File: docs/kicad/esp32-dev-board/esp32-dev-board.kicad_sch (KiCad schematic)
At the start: 6 parts, among them K1 2-Ch Relay Module, U1 ESP32 Dev Board, U2 DS18B20 Solar, U3 DS18B20 Pool

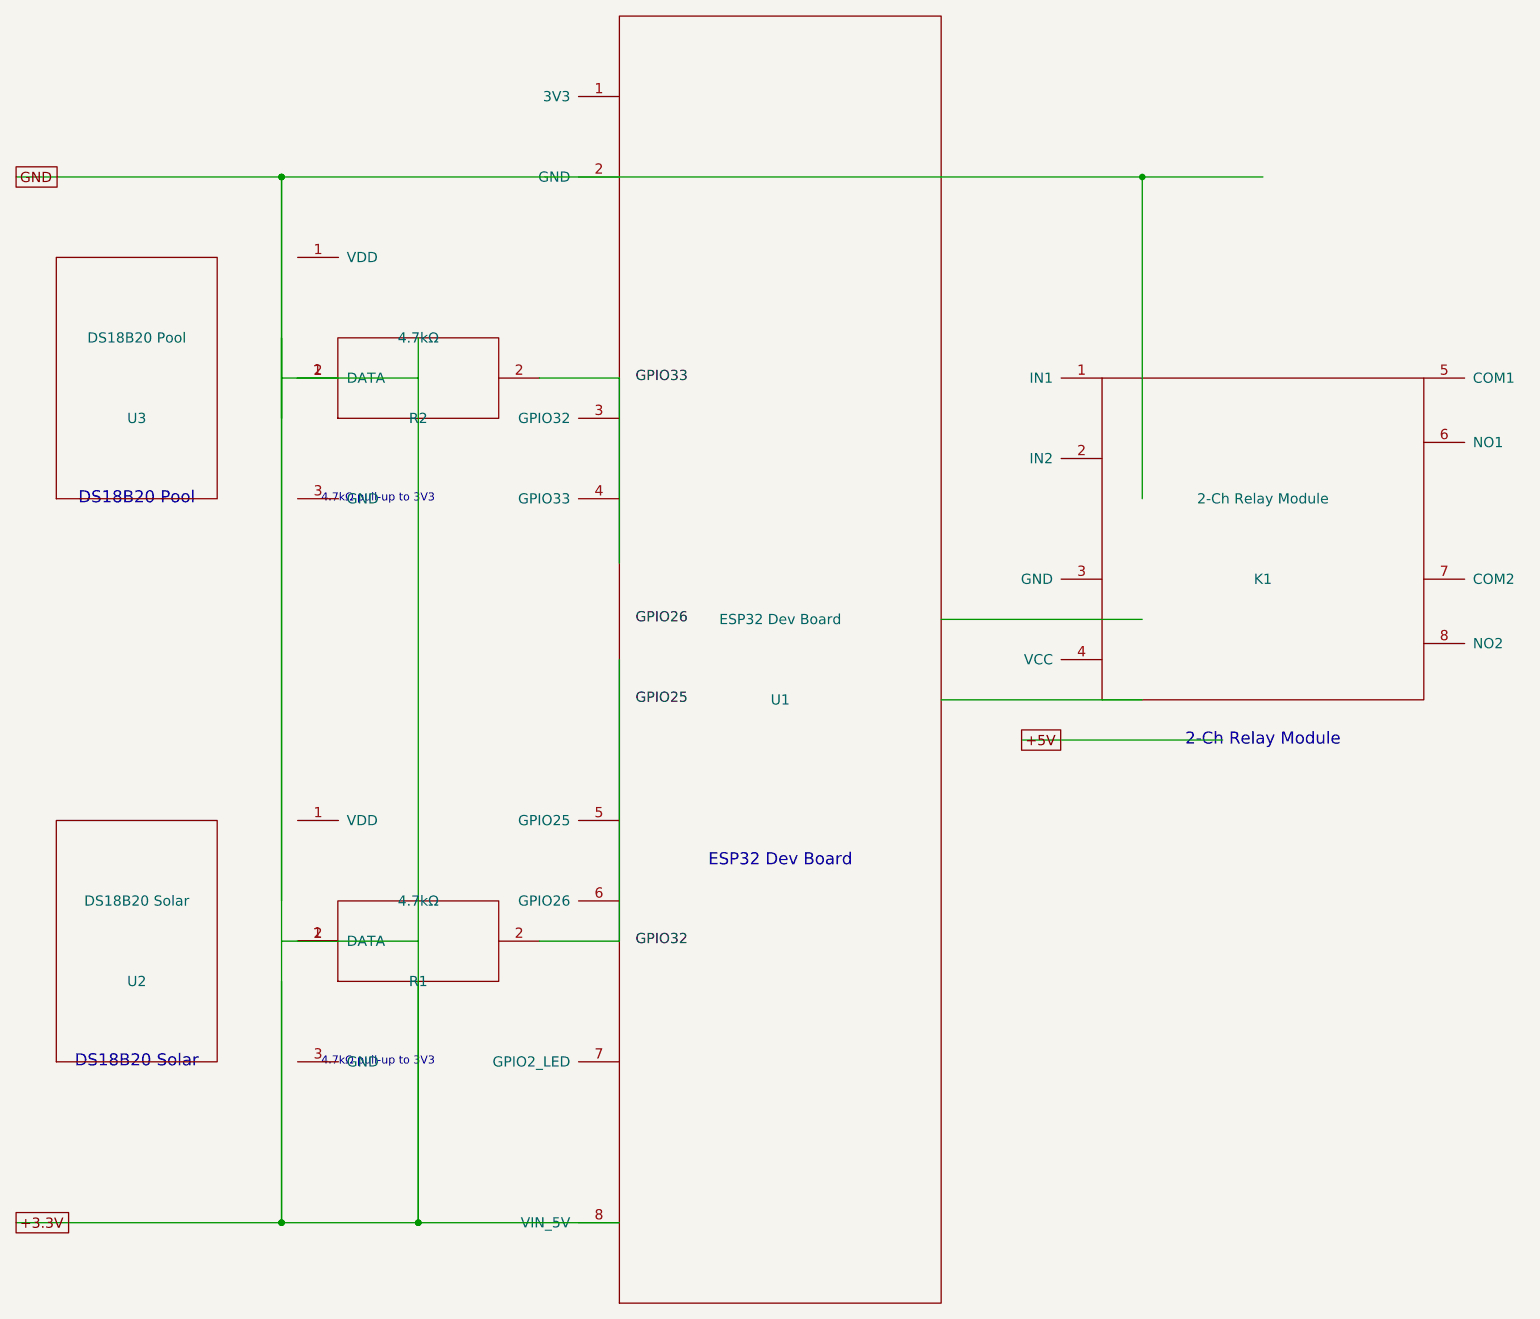
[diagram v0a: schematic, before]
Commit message: fix(docs): align KiCad schematic wires with pin coordinates after Y-axis inversion
- Add pin_tip() helper to convert local pin coordinates to absolute
  schematic positions with KiCad's Y-axis inversion
- Break power rails at each connection point so wire endpoints align
  with pin tips (fixes pin_not_connected ERC errors)
- Fix labels to match correct pin positions
- Add scripts/requirements.txt with sexpdata dependency (P2 review)
- Regenerate both variants, all remaining ERC violations are expected
  unused pins (GPIO2_LED, relay COM/NO terminals, NORVI spare GPIOs)

Fixes review P1: wire alignment with KiCad pin coordinates
Fixes review P2: sexpdata dependency declaration
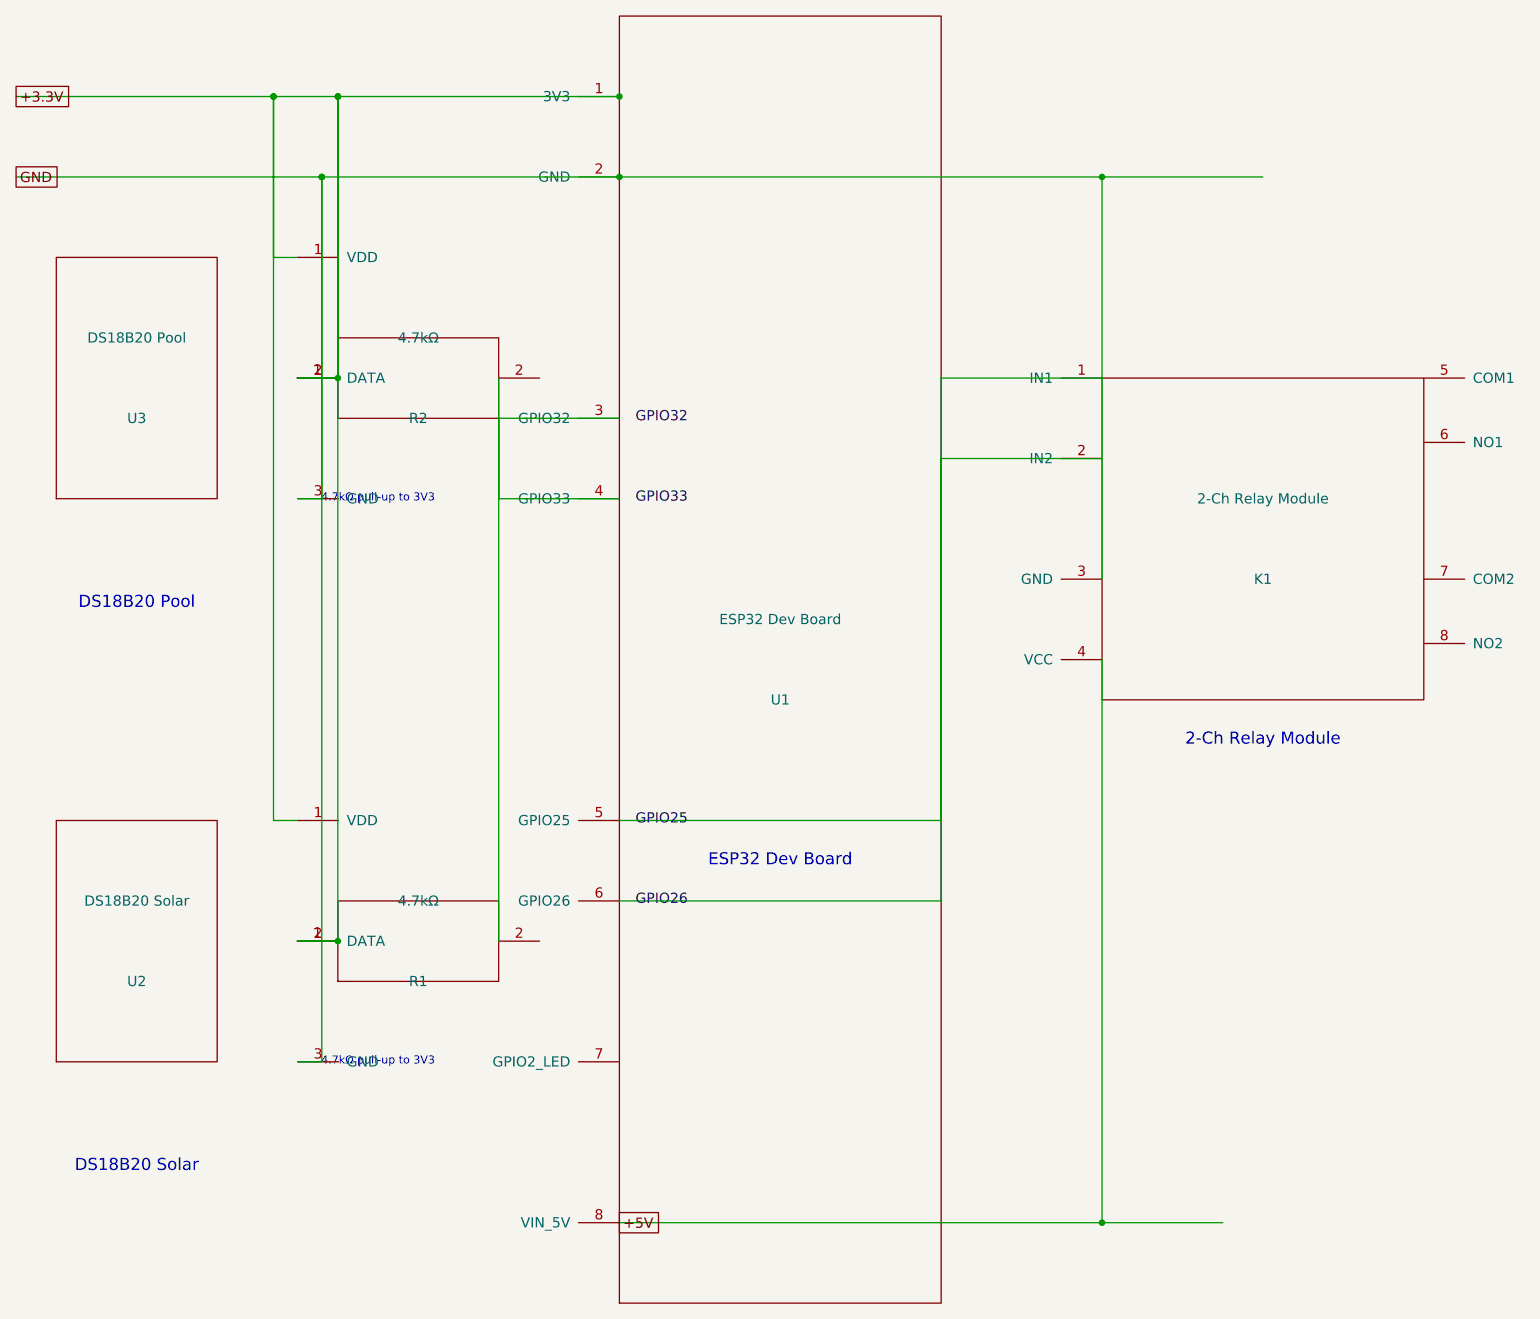
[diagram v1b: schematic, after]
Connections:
- net +3.3V: now also R1.1, R2.1, U1.1 (3V3), U2.1 (VDD), U2.2 (DATA), U3.1 (VDD), U3.2 (DATA); no longer U1.8 (VIN_5V)
- net +5V: now also K1.4 (VCC), U1.8 (VIN_5V)
- net GPIO25: now also K1.1 (IN1), K1.2 (IN2), U1.5 (GPIO25), U1.6 (GPIO26)
- net GND: now reaches U2.3 (GND)
- net GND: now also K1.3 (GND), U1.2 (GND), U3.3 (GND)
- net at U1.3 (GPIO32): now also R1.2, R2.2, U1.4 (GPIO33)
